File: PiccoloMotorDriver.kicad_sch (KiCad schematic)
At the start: 7 parts

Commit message: Started discrete inverter version
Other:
- added sheet Inverter (DRV.kicad_sch)
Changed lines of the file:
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@@
 		)
 		(instances
-			(project ""
+			(project "PiccoloMotorDriver"
 				(path "/cc8a13e7-b1a6-4cbd-adcd-4feb8b2e2369"
 					(reference "FID3")
@@
 		)
 		(instances
-			(project ""
+			(project "PiccoloMotorDriver"
 				(path "/cc8a13e7-b1a6-4cbd-adcd-4feb8b2e2369"
 					(reference "FID2")
@@
 		)
 		(instances
-			(project ""
+			(project "PiccoloMotorDriver"
 				(path "/cc8a13e7-b1a6-4cbd-adcd-4feb8b2e2369"
 					(reference "H1")
@@
 		)
 		(instances
-			(project ""
+			(project "PiccoloMotorDriver"
 				(path "/cc8a13e7-b1a6-4cbd-adcd-4feb8b2e2369"
 					(reference "FID1")
@@
 				)
 			)
+		)
+	)
+	(sheet
+		(at 120.65 72.39)
+		(size 24.13 24.13)
+		(exclude_from_sim no)
+		(in_bom yes)
+		(on_board yes)
+		(dnp no)
+		(fields_autoplaced yes)
+		(stroke
+			(width 0.1524)
+			(type solid)
+		)
+		(fill
+			(color 52 97 112 1.0000)
+		)
+		(property "Sheetname" "Inverter"
+			(at 120.65 71.6784 0)
+			(effects
+				(font
+					(size 1.27 1.27)
+				)
+				(justify left bottom)
+			)
+		)
+		(property "Sheetfile" "DRV.kicad_sch"
+			(at 120.65 97.1046 0)
+			(effects
+				(font
+					(size 1.27 1.27)
+				)
+				(justify left top)
+			)
+		)
+		(instances
+			(project "PiccoloMotorDriver"
+				(path "/cc8a13e7-b1a6-4cbd-adcd-4feb8b2e2369"
+					(page "6")
+				)
+			)

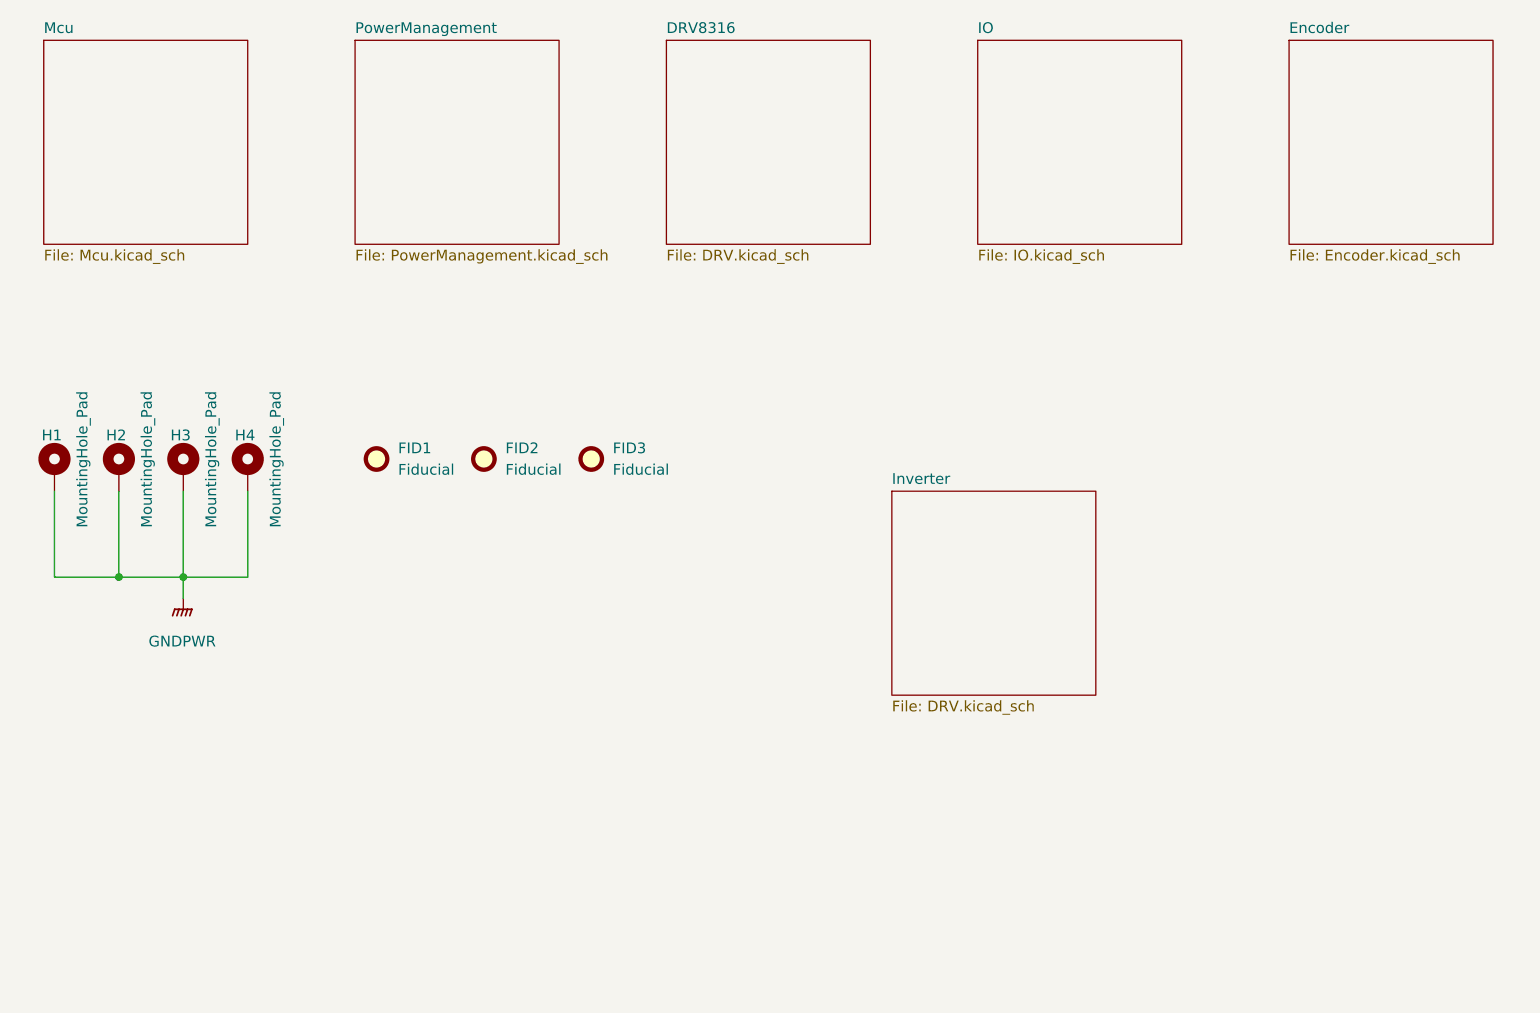
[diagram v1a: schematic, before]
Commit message: added drv8353, stm32h723vgt6
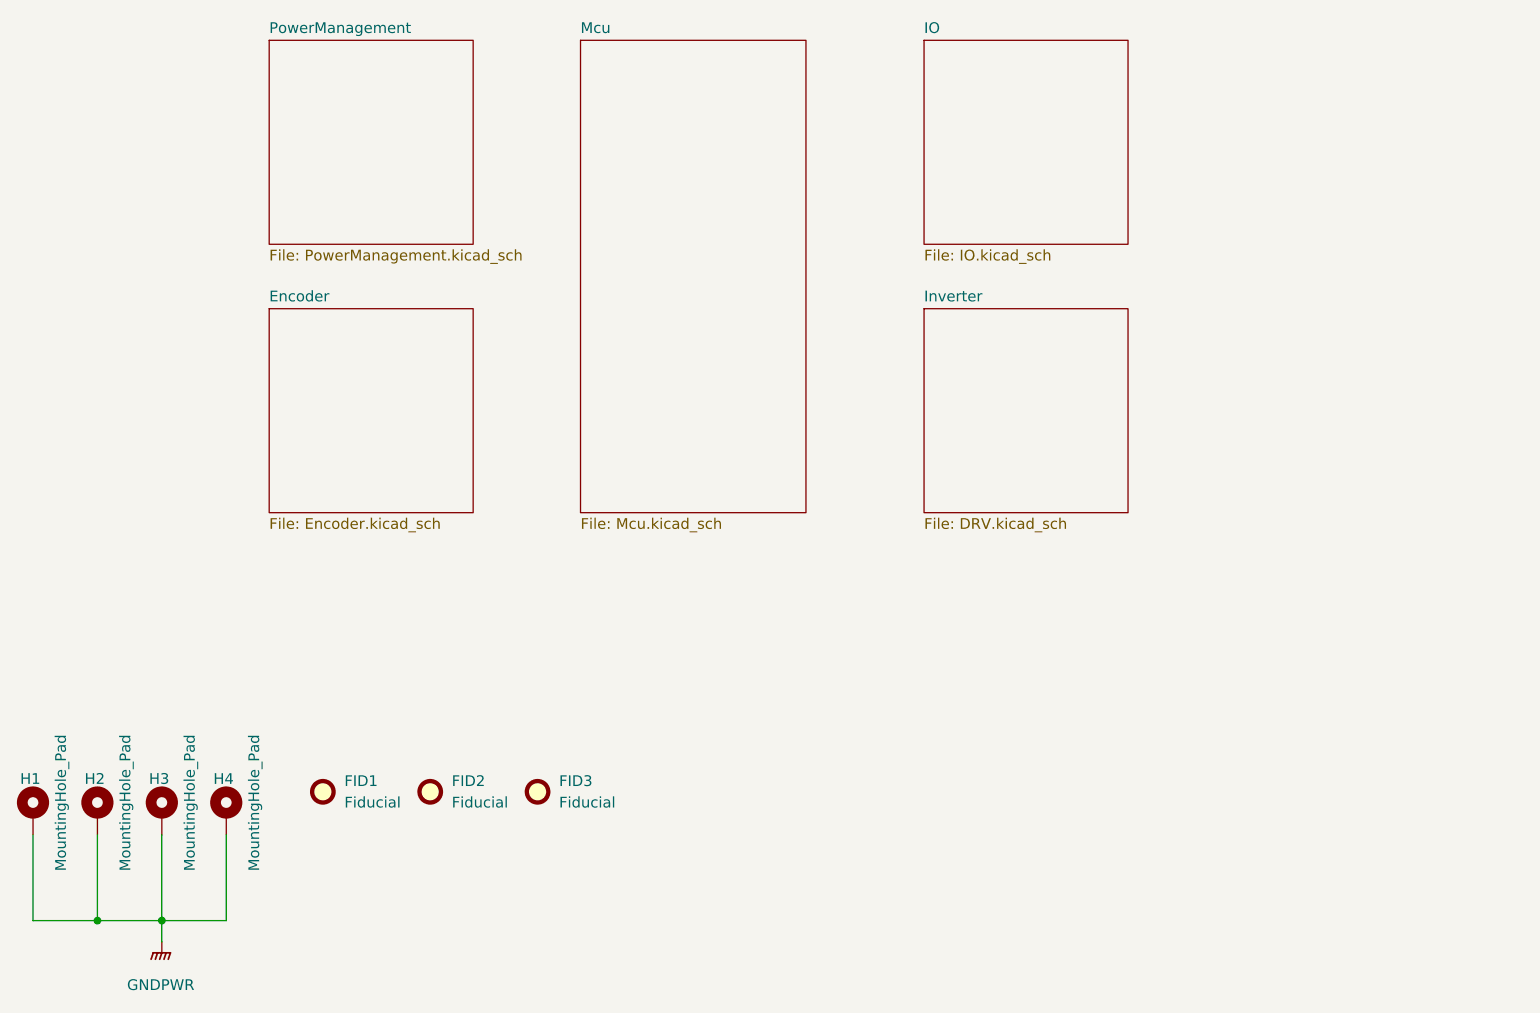
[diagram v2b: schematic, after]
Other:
- removed sheet DRV8316
- moved on the sheet: FID1, FID2, FID3, H1, H2, H3, H4
